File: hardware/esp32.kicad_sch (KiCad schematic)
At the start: 0 parts

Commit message: block refactoring
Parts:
- added C7 (x2): 1uF, Capacitor_SMD:C_0603_1608Metric, symbol Device:C
- added U2: mini_esp32, ESP32:ESP32_mini, symbol esp32:mini_esp32
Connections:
- net +3.3V: now also C7.1, U2.16 (3V3)
- net +5V: now also C7.1, U2.35 (VCC_(USB))
- net GND: now also C7.2, C7.2, U2.1 (GND), U2.22 (GND), U2.33 (GND)
- new net 1WIRE_DQ: U2.14 (IO_05/D8)
- new net AIN1: U2.11 (IO_34)
- new net AIN2: U2.7 (IO_35)
- new net DIN1: U2.31 (IO_16/D4)
- new net DIN2: U2.29 (IO_17/D3)
- new net I2C_SCL: U2.25 (IO_22/D1/SCL)
- new net I2C_SDA: U2.27 (IO_21/D2/SDA)
- new net PWM1: U2.36 (IO_02)
- no-connect marks 6 -> 25

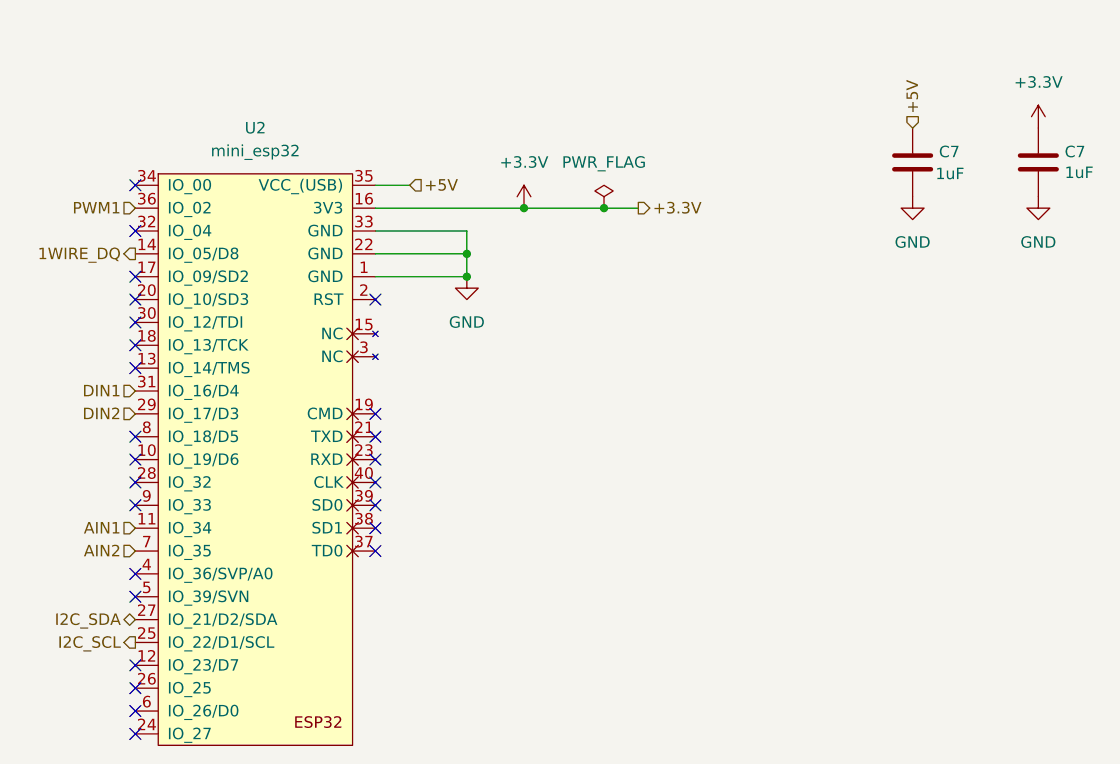
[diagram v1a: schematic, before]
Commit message: Added 3D models and ran freerouting
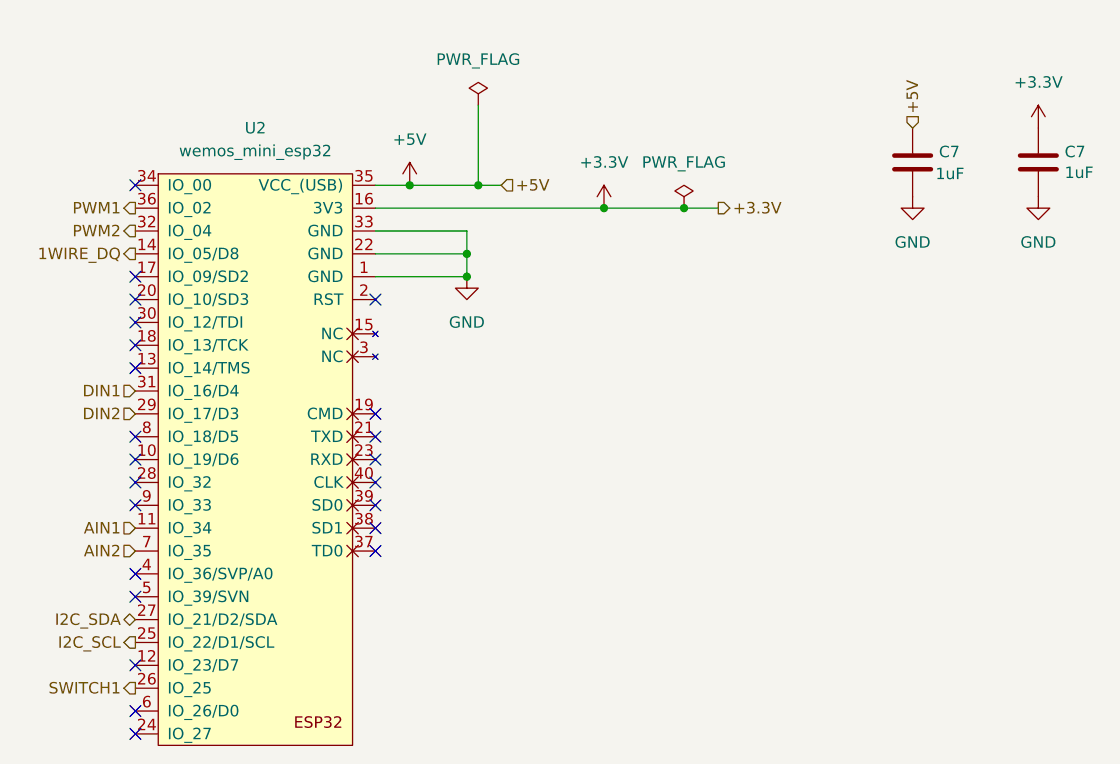
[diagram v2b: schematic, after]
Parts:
- C7: footprint Capacitor_SMD:C_0603_1608Metric -> Capacitor_SMD:C_0805_2012Metric
- U2: value mini_esp32 -> wemos_mini_esp32
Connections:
- net SWITCH1: now reaches U2.26 (IO_25)
- net PWM2: now reaches U2.32 (IO_04)
- no-connect marks 25 -> 23
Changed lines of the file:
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@@
 (kicad_sch (version 20230121) (generator eeschema)
   (paper "A4")
+  (junction (at 152.4 53.34) (diameter 0) (color 0 0 0 0)
+  )
+  (junction (at 175.26 55.88) (diameter 0) (color 0 0 0 0)
+  )
+  (junction (at 151.13 63.5) (diameter 0) (color 0 0 0 0)
+  )
+  (junction (at 151.13 60.96) (diameter 0) (color 0 0 0 0)
+  )
   (junction (at 166.37 55.88) (diameter 0) (color 0 0 0 0)
   )
-  (junction (at 151.13 63.5) (diameter 0) (color 0 0 0 0)
-  )
-  (junction (at 151.13 60.96) (diameter 0) (color 0 0 0 0)
-  )
-  (junction (at 157.48 55.88) (diameter 0) (color 0 0 0 0)
+  (junction (at 144.78 53.34) (diameter 0) (color 0 0 0 0)
   )
   (no_connect (at 114.3 88.9))
@@
   (no_connect (at 114.3 63.5))
   (no_connect (at 140.97 66.04))
-  (no_connect (at 114.3 109.22))
   (no_connect (at 114.3 106.68))
   (no_connect (at 140.97 91.44))
@@
   (no_connect (at 140.97 83.82))
   (no_connect (at 114.3 66.04))
-  (no_connect (at 114.3 58.42))
   (no_connect (at 114.3 53.34))
   (no_connect (at 114.3 81.28))
@@
   (no_connect (at 140.97 93.98))
   (no_connect (at 114.3 86.36))
-  (wire (pts (xy 170.18 55.88) (xy 166.37 55.88))
+  (wire (pts (xy 179.07 55.88) (xy 175.26 55.88))
+    (stroke (width 0) (type default))
+  )
+  (wire (pts (xy 144.78 53.34) (xy 152.4 53.34))
     (stroke (width 0) (type default))
   )
@@
     (stroke (width 0) (type default))
   )
+  (wire (pts (xy 140.97 55.88) (xy 166.37 55.88))
+    (stroke (width 0) (type default))
+  )
+  (wire (pts (xy 152.4 44.45) (xy 152.4 53.34))
+    (stroke (width 0) (type default))
+  )
+  (wire (pts (xy 152.4 53.34) (xy 154.94 53.34))
+    (stroke (width 0) (type default))
+  )
   (wire (pts (xy 140.97 63.5) (xy 151.13 63.5))
     (stroke (width 0) (type default))
@@
     (stroke (width 0) (type default))
   )
-  (wire (pts (xy 140.97 55.88) (xy 157.48 55.88))
-    (stroke (width 0) (type default))
-  )
   (wire (pts (xy 151.13 60.96) (xy 151.13 63.5))
     (stroke (width 0) (type default))
@@
     (stroke (width 0) (type default))
   )
-  (wire (pts (xy 157.48 55.88) (xy 166.37 55.88))
+  (wire (pts (xy 166.37 55.88) (xy 175.26 55.88))
     (stroke (width 0) (type default))
   )
@@
     (effects (font (size 1.27 1.27)) (justify left))
   )
-  (hierarchical_label "+3.3V" (shape output) (at 170.18 55.88 0) (fields_autoplaced)
+  (hierarchical_label "+3.3V" (shape output) (at 179.07 55.88 0) (fields_autoplaced)
     (effects (font (size 1.27 1.27)) (justify left))
   )
+  (hierarchical_label "SWITCH1" (shape output) (at 114.3 109.22 180) (fields_autoplaced)
+    (effects (font (size 1.27 1.27)) (justify right))
+  )
   (hierarchical_label "DIN1" (shape input) (at 114.3 76.2 180) (fields_autoplaced)
     (effects (font (size 1.27 1.27)) (justify right))
   )
-  (hierarchical_label "+5V" (shape input) (at 144.78 53.34 0) (fields_autoplaced)
+  (hierarchical_label "+5V" (shape input) (at 154.94 53.34 0) (fields_autoplaced)
     (effects (font (size 1.27 1.27)) (justify left))
   )
@@
     (effects (font (size 1.27 1.27)) (justify right))
   )
-  (hierarchical_label "PWM1" (shape input) (at 114.3 55.88 180) (fields_autoplaced)
+  (hierarchical_label "PWM1" (shape output) (at 114.3 55.88 180) (fields_autoplaced)
     (effects (font (size 1.27 1.27)) (justify right))
   )
@@
     (effects (font (size 1.27 1.27)) (justify right))
   )
+  (hierarchical_label "PWM2" (shape output) (at 114.3 58.42 180) (fields_autoplaced)
+    (effects (font (size 1.27 1.27)) (justify right))
+  )
   (hierarchical_label "I2C_SCL" (shape output) (at 114.3 104.14 180) (fields_autoplaced)
     (effects (font (size 1.27 1.27)) (justify right))
@@
         (path "/3d8a08e7-1222-4d27-bd08-b4e997cf9472/01b79695-c7e6-49b6-b47f-2bc3bf2a333c"
           (reference "#PWR010") (unit 1)
+        )
+      )
+    )
+  )
+  (symbol (lib_id "power:PWR_FLAG") (at 152.4 44.45 0) (unit 1)
+    (in_bom yes) (on_board yes) (dnp no) (fields_autoplaced)
+    (property "Reference" "#FLG01" (at 152.4 42.545 0)
+      (effects (font (size 1.27 1.27)) hide)
+    )
+    (property "Value" "PWR_FLAG" (at 152.4 39.37 0)
+      (effects (font (size 1.27 1.27)))
+    )
+    (property "Footprint" "" (at 152.4 44.45 0)
+      (effects (font (size 1.27 1.27)) hide)
+    )
+    (property "Datasheet" "~" (at 152.4 44.45 0)
+      (effects (font (size 1.27 1.27)) hide)
+    )
+    (pin "1")
+    (instances
+      (project "esp32-multitool"
+        (path "/3d8a08e7-1222-4d27-bd08-b4e997cf9472/01b79695-c7e6-49b6-b47f-2bc3bf2a333c"
+          (reference "#FLG01") (unit 1)
         )
       )
@@
         (path "/3d8a08e7-1222-4d27-bd08-b4e997cf9472/01b79695-c7e6-49b6-b47f-2bc3bf2a333c"
           (reference "#PWR09") (unit 1)
+        )
+      )
+    )
+  )
+  (symbol (lib_id "power:+5V") (at 144.78 53.34 0) (unit 1)
+    (in_bom yes) (on_board yes) (dnp no) (fields_autoplaced)
+    (property "Reference" "#PWR01" (at 144.78 57.15 0)
+      (effects (font (size 1.27 1.27)) hide)
+    )
+    (property "Value" "+5V" (at 144.78 48.26 0)
+      (effects (font (size 1.27 1.27)))
+    )
+    (property "Footprint" "" (at 144.78 53.34 0)
+      (effects (font (size 1.27 1.27)) hide)
+    )
+    (property "Datasheet" "" (at 144.78 53.34 0)
+      (effects (font (size 1.27 1.27)) hide)
+    )
+    (pin "1")
+    (instances
+      (project "esp32-multitool"
+        (path "/3d8a08e7-1222-4d27-bd08-b4e997cf9472/01b79695-c7e6-49b6-b47f-2bc3bf2a333c"
+          (reference "#PWR01") (unit 1)
         )
       )
@@
       (effects (font (size 1.27 1.27)) (justify left))
     )
-    (property "Footprint" "Capacitor_SMD:C_0603_1608Metric" (at 201.6252 54.61 0)
+    (property "Footprint" "Capacitor_SMD:C_0805_2012Metric" (at 201.6252 54.61 0)
       (effects (font (size 1.27 1.27)) hide)
     )
@@
     )
   )
-  (symbol (lib_id "power:+3.3V") (at 157.48 55.88 0) (unit 1)
+  (symbol (lib_id "power:+3.3V") (at 166.37 55.88 0) (unit 1)
     (in_bom yes) (on_board yes) (dnp no)
-    (property "Reference" "#PWR04" (at 157.48 59.69 0)
-      (effects (font (size 1.27 1.27)) hide)
-    )
-    (property "Value" "+3.3V" (at 157.48 50.8 0)
-      (effects (font (size 1.27 1.27)))
-    )
-    (property "Footprint" "" (at 157.48 55.88 0)
-      (effects (font (size 1.27 1.27)) hide)
-    )
-    (property "Datasheet" "" (at 157.48 55.88 0)
+    (property "Reference" "#PWR04" (at 166.37 59.69 0)
+      (effects (font (size 1.27 1.27)) hide)
+    )
+    (property "Value" "+3.3V" (at 166.37 50.8 0)
+      (effects (font (size 1.27 1.27)))
+    )
+    (property "Footprint" "" (at 166.37 55.88 0)
+      (effects (font (size 1.27 1.27)) hide)
+    )
+    (property "Datasheet" "" (at 166.37 55.88 0)
       (effects (font (size 1.27 1.27)) hide)
     )
@@
       (effects (font (size 1.27 1.27)) (justify left))
     )
-    (property "Footprint" "Capacitor_SMD:C_0603_1608Metric" (at 215.5952 54.61 0)
+    (property "Footprint" "Capacitor_SMD:C_0805_2012Metric" (at 215.5952 54.61 0)
       (effects (font (size 1.27 1.27)) hide)
     )
@@
       (effects (font (size 1.27 1.27)))
     )
-    (property "Value" "mini_esp32" (at 127.635 49.53 0)
+    (property "Value" "wemos_mini_esp32" (at 127.635 49.53 0)
       (effects (font (size 1.27 1.27)))
     )
@@
     )
   )
-  (symbol (lib_id "power:PWR_FLAG") (at 166.37 55.88 0) (unit 1)
-    (in_bom yes) (on_board yes) (dnp no) (fields_autoplaced)
-    (property "Reference" "#FLG04" (at 166.37 53.975 0)
-      (effects (font (size 1.27 1.27)) hide)
-    )
-    (property "Value" "PWR_FLAG" (at 166.37 50.8 0)
-      (effects (font (size 1.27 1.27)))
-    )
-    (property "Footprint" "" (at 166.37 55.88 0)
-      (effects (font (size 1.27 1.27)) hide)
-    )
-    (property "Datasheet" "~" (at 166.37 55.88 0)
-      (effects (font (size 1.27 1.27)) hide)
-    )
+  (symbol (lib_id "power:PWR_FLAG") (at 175.26 55.88 0) (unit 1)
+    (in_bom yes) (on_board yes) (dnp no) (fields_autoplaced)
+    (property "Reference" "#FLG04" (at 175.26 53.975 0)
+      (effects (font (size 1.27 1.27)) hide)
+    )
+    (property "Value" "PWR_FLAG" (at 175.26 50.8 0)
+      (effects (font (size 1.27 1.27)))
+    )
+    (property "Footprint" "" (at 175.26 55.88 0)
+      (effects (font (size 1.27 1.27)) hide)
+    )
+    (property "Datasheet" "~" (at 175.26 55.88 0)
+      (effects (font (size 1.27 1.27)) hide)
+    )
